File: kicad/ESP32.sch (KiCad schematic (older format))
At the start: 30 parts

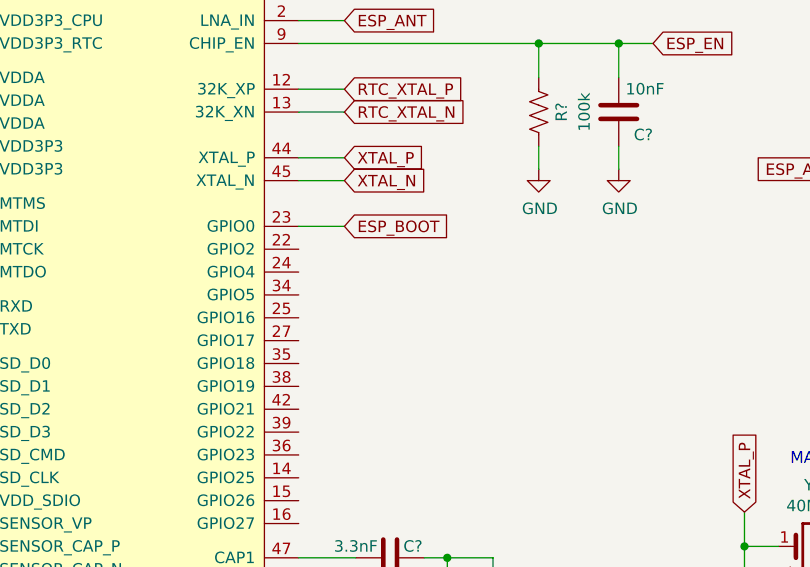
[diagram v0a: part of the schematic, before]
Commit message: 3 output SMPS added MIC23450
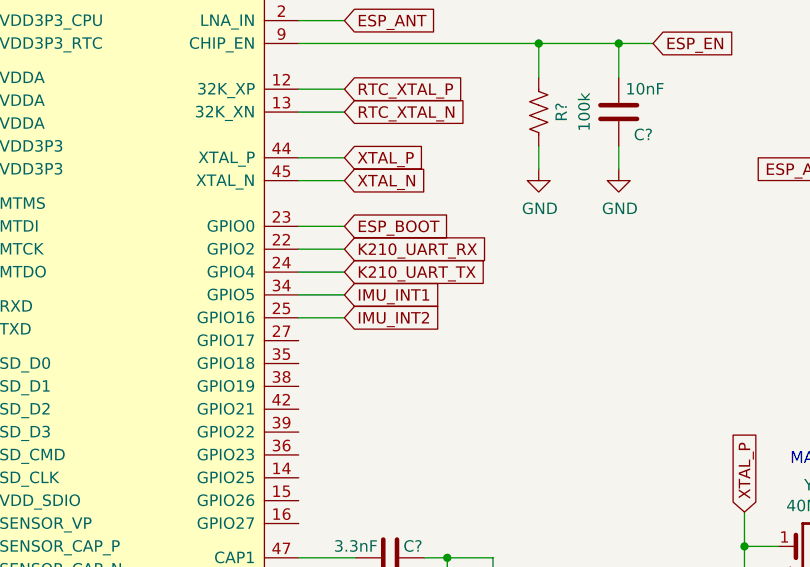
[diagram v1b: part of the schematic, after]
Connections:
- net K210_UART_RX: now reaches U?.22 (GPIO2)
- net K210_UART_TX: now reaches U?.24 (GPIO4)
- net IMU_INT2: now reaches U?.25 (GPIO16)
- net IMU_INT1: now reaches U?.34 (GPIO5)
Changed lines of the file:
@@
 $Descr A4 11693 8268
 encoding utf-8
-Sheet 4 4
+Sheet 4 5
 Title ""
 Date ""
@@
 Wire Wire Line
 	1550 5100 1550 5050
+Text GLabel 6800 3600 2    50   Input ~ 0
+K210_UART_RX
+Text GLabel 6800 3700 2    50   Input ~ 0
+K210_UART_TX
+Wire Wire Line
+	6800 3700 6600 3700
+Wire Wire Line
+	6600 3600 6800 3600
+Text GLabel 6800 3800 2    50   Input ~ 0
+IMU_INT1
+Text GLabel 6800 3900 2    50   Input ~ 0
+IMU_INT2
+Wire Wire Line
+	6800 3800 6600 3800
+Wire Wire Line
+	6600 3900 6800 3900
 Wire Bus Line
 	4250 4200 4250 4700
